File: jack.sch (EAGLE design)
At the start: 16 parts, among them IC1 NUF2221W1T2G

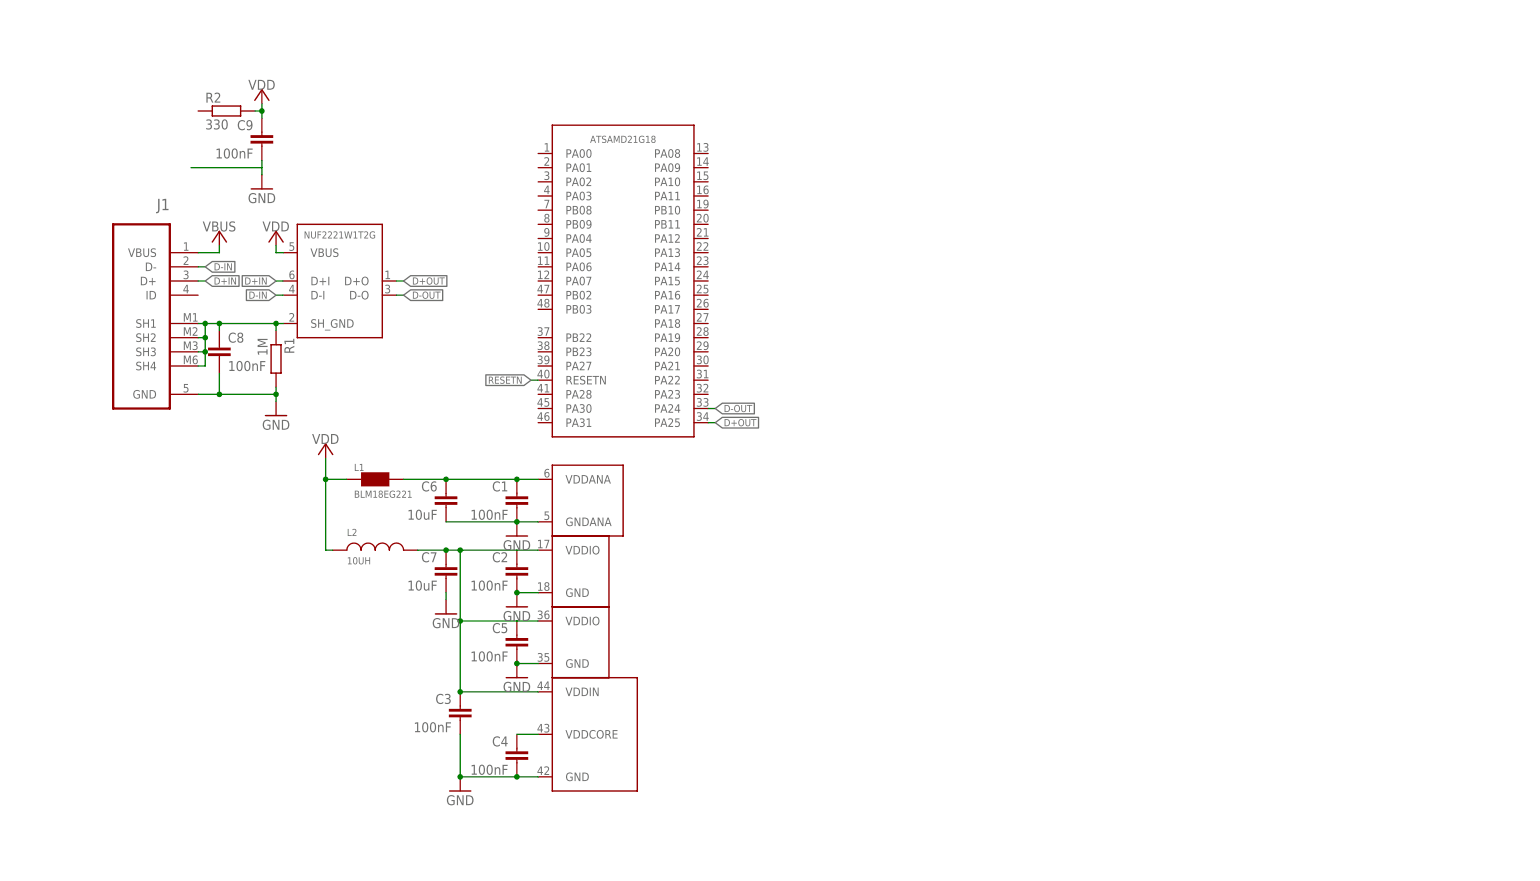
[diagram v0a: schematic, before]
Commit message: :grin: Added SPST symbol, modded SAMD21 pin names
Added SPST symbol for the reset switch (still got to find a suitable
tact switch), modified the SAMD21 pin names to show all their functions
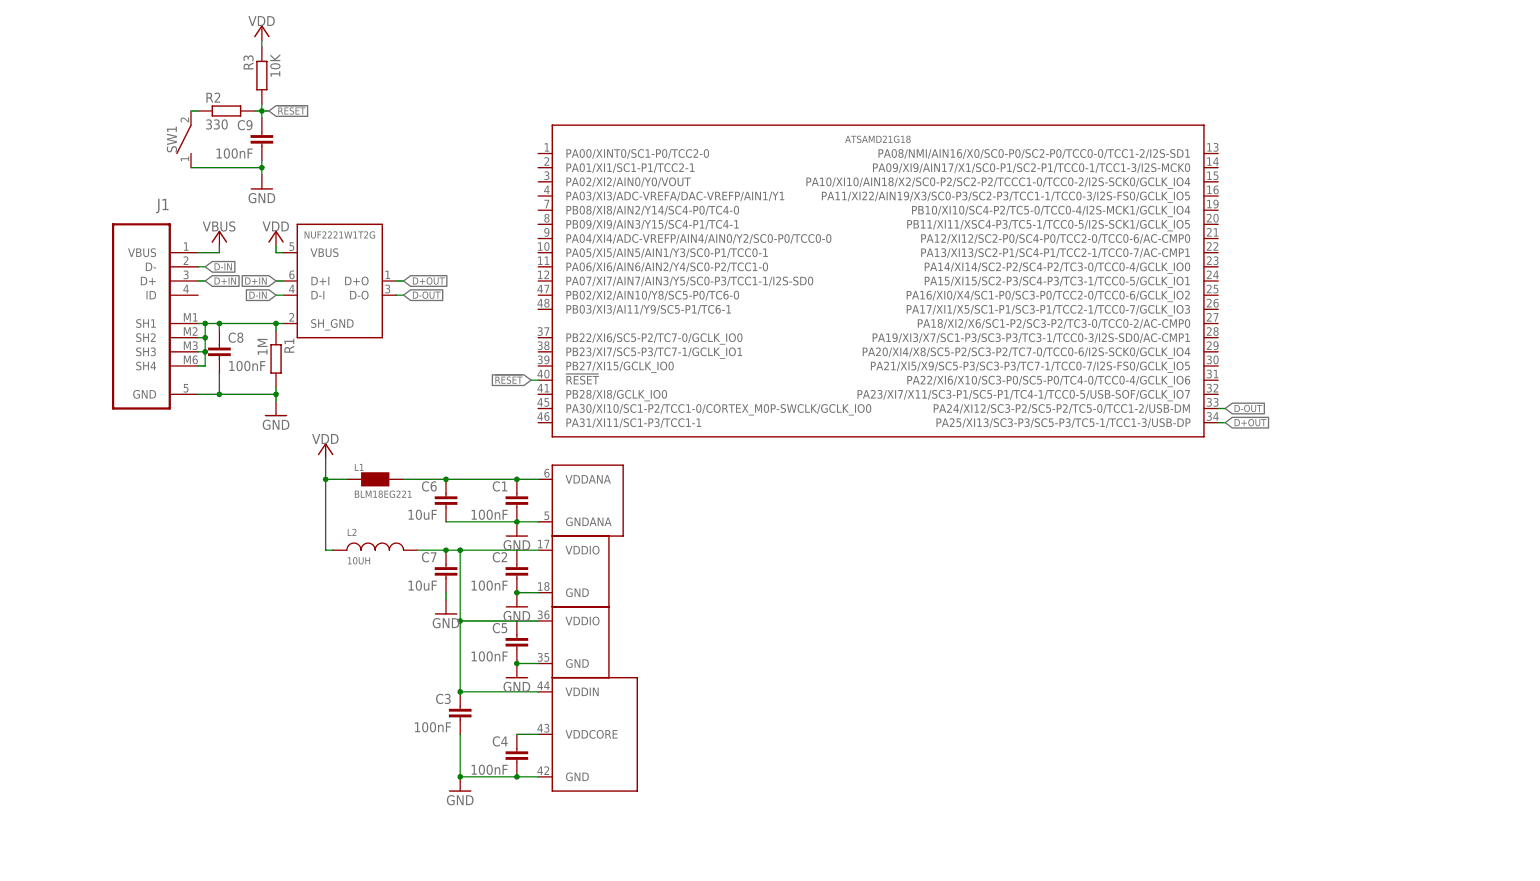
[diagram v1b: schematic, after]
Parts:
- removed U$1: ATSAMD21G18, jack:ATSAMD21G18
- added IC2: ATSAMD21G18, jack:ATSAMD21G18
- added R3: 10K, rcl:R-EU_R0603
- added SW1: SPST, jack:SPST
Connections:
- removed net RESETN: U$1IO.RESETN
- new net !RESET: C9.1, IC2IO.!RESET, R2.2, R3.2
- new net N$3: R2.1, SW1.P$2
- net D+OUT: now also IC2IO.PA25/XI13/SC3-P3/SC5-P3/TC5-1/TCC1-3/USB-DP; no longer U$1IO.PA25
- net D-OUT: now also IC2IO.PA24/XI12/SC3-P2/SC5-P2/TC5-0/TCC1-2/USB-DM; no longer U$1IO.PA24
- net GND: now also IC2PWR-ANA.GNDANA, IC2PWR-IN-CORE.GND, IC2PWR-IO1.GND, IC2PWR-IO2.GND, SW1.P$1; no longer U$1PWR-ANA.GNDANA, U$1PWR-IN-CORE.GND, U$1PWR-IO1.GND, U$1PWR-IO2.GND
- net N$1: now also IC2PWR-ANA.VDDANA; no longer U$1PWR-ANA.VDDANA
- net N$4: now also IC2PWR-IN-CORE.VDDIN, IC2PWR-IO1.VDDIO, IC2PWR-IO2.VDDIO; no longer U$1PWR-IN-CORE.VDDIN, U$1PWR-IO1.VDDIO, U$1PWR-IO2.VDDIO
- net VDD: now also R3.1; no longer C9.1, R2.2
- net VDDCORE: now also IC2PWR-IN-CORE.VDDCORE; no longer U$1PWR-IN-CORE.VDDCORE
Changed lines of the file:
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@@
 </classes>
 <parts>
-<part name="U$1" library="jack" deviceset="ATSAMD21G18" device=""/>
+<part name="IC2" library="jack" deviceset="ATSAMD21G18" device=""/>
 <part name="C1" library="rcl" deviceset="C-EU" device="C0603" value="100nF"/>
 <part name="C2" library="rcl" deviceset="C-EU" device="C0603" value="100nF"/>
@@
 <part name="GND7" library="cortexm0" deviceset="GND" device=""/>
 <part name="R2" library="rcl" deviceset="R-EU_" device="R0603" value="330"/>
+<part name="R3" library="rcl" deviceset="R-EU_" device="R0603" value="10K"/>
+<part name="SW1" library="jack" deviceset="SPST" device=""/>
 </parts>
 <sheets>
@@
 </plain>
 <instances>
-<instance part="U$1" gate="IO" x="0" y="0"/>
-<instance part="U$1" gate="PWR-ANA" x="-6.35" y="-39.37"/>
-<instance part="U$1" gate="PWR-IN-CORE" x="-5.08" y="-81.28"/>
-<instance part="U$1" gate="PWR-IO1" x="-7.62" y="-52.07"/>
-<instance part="U$1" gate="PWR-IO2" x="-7.62" y="-64.77"/>
+<instance part="IC2" gate="IO" x="45.72" y="0"/>
+<instance part="IC2" gate="PWR-ANA" x="-6.35" y="-39.37"/>
+<instance part="IC2" gate="PWR-IN-CORE" x="-5.08" y="-81.28"/>
+<instance part="IC2" gate="PWR-IO1" x="-7.62" y="-52.07"/>
+<instance part="IC2" gate="PWR-IO2" x="-7.62" y="-64.77"/>
 <instance part="C1" gate="G$1" x="-19.05" y="-38.1" rot="MR0"/>
 <instance part="C2" gate="G$1" x="-19.05" y="-50.8" rot="MR0"/>
@@
 <instance part="GND6" gate="G$1" x="-62.23" y="-21.59"/>
 <instance part="C9" gate="G$1" x="-64.77" y="26.67" rot="MR0"/>
-<instance part="VDD3" gate="G$1" x="-64.77" y="31.75"/>
+<instance part="VDD3" gate="G$1" x="-64.77" y="43.18"/>
 <instance part="GND7" gate="G$1" x="-64.77" y="19.05"/>
 <instance part="R2" gate="G$1" x="-71.12" y="30.48"/>
+<instance part="R3" gate="G$1" x="-64.77" y="36.83" rot="MR270"/>
+<instance part="SW1" gate="G$1" x="-77.47" y="25.4" rot="R90"/>
 </instances>
 <busses>
@@
 <net name="GND" class="0">
 <segment>
-<pinref part="U$1" gate="PWR-IO1" pin="GND"/>
+<pinref part="IC2" gate="PWR-IO1" pin="GND"/>
 <pinref part="C2" gate="G$1" pin="2"/>
 <wire x1="-15.24" y1="-55.88" x2="-19.05" y2="-55.88" width="0.1524" layer="91"/>
@@
 </segment>
 <segment>
-<pinref part="U$1" gate="PWR-IO2" pin="GND"/>
+<pinref part="IC2" gate="PWR-IO2" pin="GND"/>
 <pinref part="C5" gate="G$1" pin="2"/>
 <wire x1="-15.24" y1="-68.58" x2="-19.05" y2="-68.58" width="0.1524" layer="91"/>
@@
 </segment>
 <segment>
-<pinref part="U$1" gate="PWR-IN-CORE" pin="GND"/>
+<pinref part="IC2" gate="PWR-IN-CORE" pin="GND"/>
 <pinref part="C4" gate="G$1" pin="2"/>
 <wire x1="-15.24" y1="-88.9" x2="-19.05" y2="-88.9" width="0.1524" layer="91"/>
@@
 </segment>
 <segment>
-<pinref part="U$1" gate="PWR-ANA" pin="GNDANA"/>
+<pinref part="IC2" gate="PWR-ANA" pin="GNDANA"/>
 <pinref part="C1" gate="G$1" pin="2"/>
 <wire x1="-15.24" y1="-43.18" x2="-19.05" y2="-43.18" width="0.1524" layer="91"/>
@@
 <wire x1="-64.77" y1="20.32" x2="-64.77" y2="19.05" width="0.1524" layer="91"/>
 <wire x1="-64.77" y1="20.32" x2="-77.47" y2="20.32" width="0.1524" layer="91"/>
+<junction x="-64.77" y="20.32"/>
+<pinref part="SW1" gate="G$1" pin="P$1"/>
 </segment>
 </net>
 <net name="VDDCORE" class="0">
 <segment>
-<pinref part="U$1" gate="PWR-IN-CORE" pin="VDDCORE"/>
+<pinref part="IC2" gate="PWR-IN-CORE" pin="VDDCORE"/>
 <pinref part="C4" gate="G$1" pin="1"/>
 <wire x1="-15.24" y1="-81.28" x2="-19.05" y2="-81.28" width="0.1524" layer="91"/>
@@
 </segment>
 <segment>
-<pinref part="C9" gate="G$1" pin="1"/>
 <pinref part="VDD3" gate="G$1" pin="VDD"/>
-<wire x1="-64.77" y1="31.75" x2="-64.77" y2="30.48" width="0.1524" layer="91"/>
-<pinref part="R2" gate="G$1" pin="2"/>
-<wire x1="-64.77" y1="30.48" x2="-64.77" y2="29.21" width="0.1524" layer="91"/>
-<wire x1="-66.04" y1="30.48" x2="-64.77" y2="30.48" width="0.1524" layer="91"/>
-<junction x="-64.77" y="30.48"/>
+<pinref part="R3" gate="G$1" pin="1"/>
+<wire x1="-64.77" y1="43.18" x2="-64.77" y2="41.91" width="0.1524" layer="91"/>
 </segment>
 </net>
 <net name="N$1" class="0">
 <segment>
-<pinref part="U$1" gate="PWR-ANA" pin="VDDANA"/>
+<pinref part="IC2" gate="PWR-ANA" pin="VDDANA"/>
 <pinref part="C1" gate="G$1" pin="1"/>
 <wire x1="-15.24" y1="-35.56" x2="-19.05" y2="-35.56" width="0.1524" layer="91"/>
@@
 <net name="N$4" class="0">
 <segment>
-<pinref part="U$1" gate="PWR-IO2" pin="VDDIO"/>
+<pinref part="IC2" gate="PWR-IO2" pin="VDDIO"/>
 <pinref part="C5" gate="G$1" pin="1"/>
 <wire x1="-15.24" y1="-60.96" x2="-19.05" y2="-60.96" width="0.1524" layer="91"/>
@@
 <pinref part="C7" gate="G$1" pin="1"/>
 <wire x1="-31.75" y1="-48.26" x2="-36.83" y2="-48.26" width="0.1524" layer="91"/>
-<pinref part="U$1" gate="PWR-IO1" pin="VDDIO"/>
+<pinref part="IC2" gate="PWR-IO1" pin="VDDIO"/>
 <pinref part="C2" gate="G$1" pin="1"/>
 <wire x1="-15.24" y1="-48.26" x2="-19.05" y2="-48.26" width="0.1524" layer="91"/>
@@
 <wire x1="-29.21" y1="-48.26" x2="-19.05" y2="-48.26" width="0.1524" layer="91"/>
 <wire x1="-29.21" y1="-60.96" x2="-29.21" y2="-48.26" width="0.1524" layer="91"/>
-<pinref part="U$1" gate="PWR-IN-CORE" pin="VDDIN"/>
+<pinref part="IC2" gate="PWR-IN-CORE" pin="VDDIN"/>
 <pinref part="C3" gate="G$1" pin="1"/>
 <wire x1="-15.24" y1="-73.66" x2="-29.21" y2="-73.66" width="0.1524" layer="91"/>
@@
 <net name="D+OUT" class="0">
 <segment>
-<pinref part="U$1" gate="IO" pin="PA25"/>
-<wire x1="15.24" y1="-25.4" x2="16.51" y2="-25.4" width="0.1524" layer="91"/>
-<label x="16.51" y="-25.4" size="1.27" layer="95" xref="yes"/>
-</segment>
-<segment>
 <wire x1="-40.64" y1="0" x2="-39.37" y2="0" width="0.1524" layer="91"/>
 <label x="-39.37" y="0" size="1.27" layer="95" xref="yes"/>
 <pinref part="IC1" gate="G$1" pin="D+O"/>
 </segment>
+<segment>
+<pinref part="IC2" gate="IO" pin="PA25/XI13/SC3-P3/SC5-P3/TC5-1/TCC1-3/USB-DP"/>
+<wire x1="106.68" y1="-25.4" x2="107.95" y2="-25.4" width="0.1524" layer="91"/>
+<label x="107.95" y="-25.4" size="1.27" layer="95" xref="yes"/>
+</segment>
 </net>
 <net name="D-OUT" class="0">
-<segment>
-<pinref part="U$1" gate="IO" pin="PA24"/>
-<wire x1="15.24" y1="-22.86" x2="16.51" y2="-22.86" width="0.1524" layer="91"/>
-<label x="16.51" y="-22.86" size="1.27" layer="95" xref="yes"/>
-</segment>
 <segment>
 <wire x1="-40.64" y1="-2.54" x2="-39.37" y2="-2.54" width="0.1524" layer="91"/>
 <label x="-39.37" y="-2.54" size="1.27" layer="95" xref="yes"/>
 <pinref part="IC1" gate="G$1" pin="D-O"/>
+</segment>
+<segment>
+<pinref part="IC2" gate="IO" pin="PA24/XI12/SC3-P2/SC5-P2/TC5-0/TCC1-2/USB-DM"/>
+<wire x1="106.68" y1="-22.86" x2="107.95" y2="-22.86" width="0.1524" layer="91"/>
+<label x="107.95" y="-22.86" size="1.27" layer="95" xref="yes"/>
 </segment>
 </net>
@@
 </segment>
 </net>
-<net name="RESETN" class="0">
-<segment>
-<pinref part="U$1" gate="IO" pin="RESETN"/>
+<net name="!RESET" class="0">
+<segment>
+<pinref part="IC2" gate="IO" pin="!RESET"/>
 <wire x1="-15.24" y1="-17.78" x2="-16.51" y2="-17.78" width="0.1524" layer="91"/>
 <label x="-16.51" y="-17.78" size="1.27" layer="95" rot="R180" xref="yes"/>
 </segment>
-</net>
+<segment>
+<pinref part="C9" gate="G$1" pin="1"/>
+<pinref part="R2" gate="G$1" pin="2"/>
+<wire x1="-64.77" y1="30.48" x2="-64.77" y2="29.21" width="0.1524" layer="91"/>
+<wire x1="-66.04" y1="30.48" x2="-64.77" y2="30.48" width="0.1524" layer="91"/>
+<junction x="-64.77" y="30.48"/>
+<wire x1="-64.77" y1="30.48" x2="-63.5" y2="30.48" width="0.1524" layer="91"/>
+<pinref part="R3" gate="G$1" pin="2"/>
+<wire x1="-64.77" y1="31.75" x2="-64.77" y2="30.48" width="0.1524" layer="91"/>
+<label x="-63.5" y="30.48" size="1.27" layer="95" xref="yes"/>
+</segment>
+</net>
+<net name="N$3" class="0">
+<segment>
+<pinref part="R2" gate="G$1" pin="1"/>
+<wire x1="-76.2" y1="30.48" x2="-77.47" y2="30.48" width="0.1524" layer="91"/>
+<pinref part="SW1" gate="G$1" pin="P$2"/>
+</segment>
+</net>

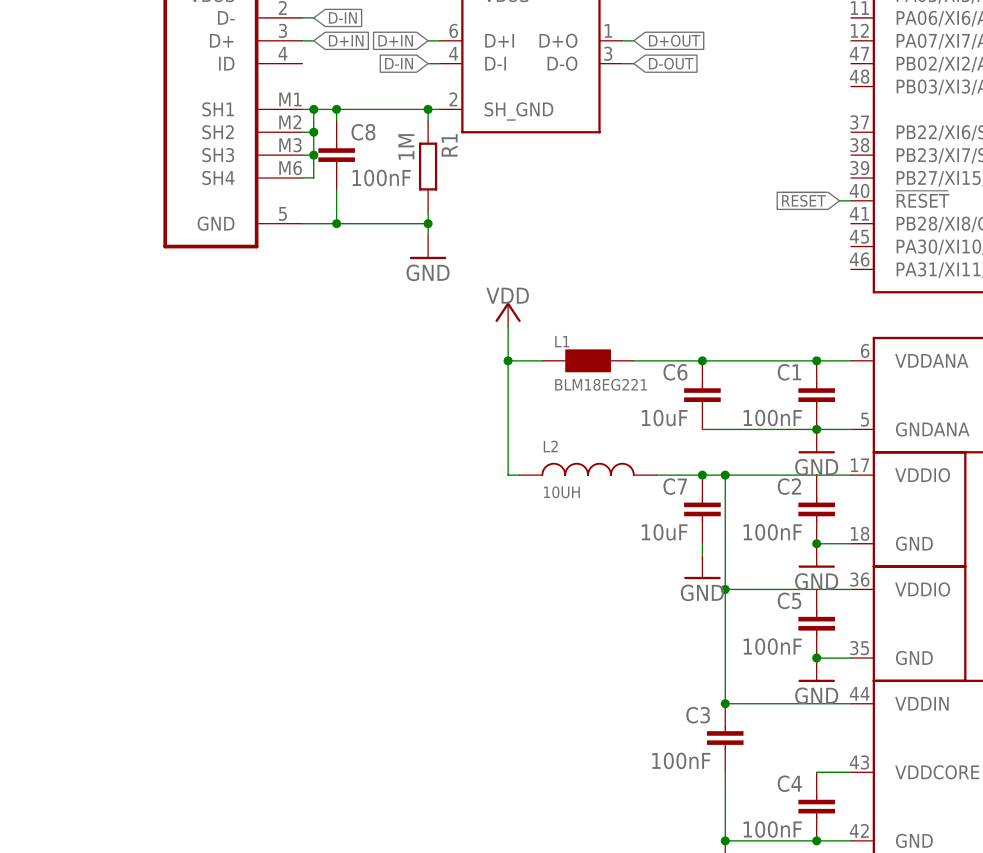
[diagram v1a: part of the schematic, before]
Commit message: :+1:  Added LDO and graphics
Added 3.3 V LDO in library and schematic, added graphics for logo
(temporary?)
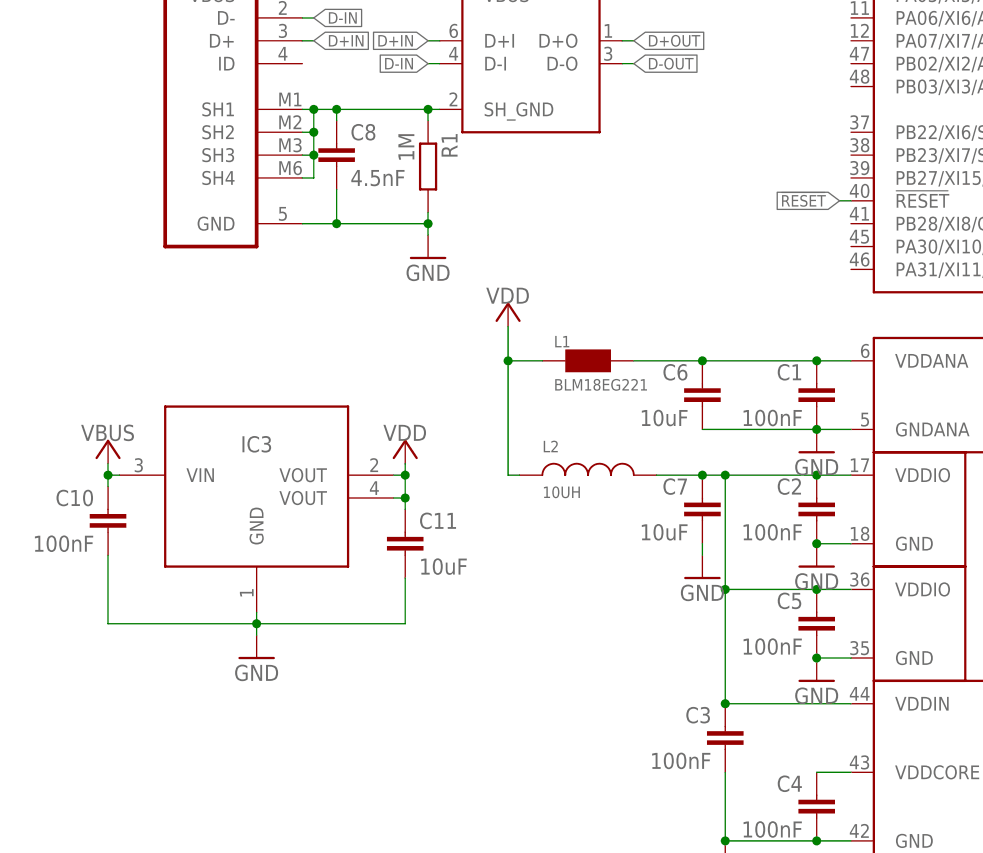
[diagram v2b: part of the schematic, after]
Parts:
- added C10: 100nF, rcl:C-EUC0603
- added C11: 10uF, rcl:C-EUC0603
- added IC3: LDO, jack:LDO
- C8: value 100nF -> 4.5nF
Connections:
- net GND: now also C10.2, C11.2, IC3.GND
- net VBUS: now also C10.1, IC3.VIN
- net VDD: now also C11.1, IC3.VOUT@1, IC3.VOUT@2
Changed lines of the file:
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@@
 <part name="L2" library="Panasonic-ELL" deviceset="ELL" device="-VXG" technology="VFG100MC" value="10UH"/>
 <part name="J1" library="Molex-47346-0001" deviceset="47346-0001" device=""/>
-<part name="C8" library="rcl" deviceset="C-EU" device="C0603" value="100nF"/>
+<part name="C8" library="rcl" deviceset="C-EU" device="C0603" value="4.5nF"/>
 <part name="R1" library="rcl" deviceset="R-EU_" device="R0603" value="1M"/>
 <part name="IC1" library="jack" deviceset="NUF2221W1T2G" device=""/>
@@
 <part name="R3" library="rcl" deviceset="R-EU_" device="R0603" value="10K"/>
 <part name="SW1" library="jack" deviceset="SPST" device=""/>
+<part name="IC3" library="jack" deviceset="LDO" device=""/>
+<part name="VDD4" library="jack" deviceset="VDD" device=""/>
+<part name="VBUS2" library="jack" deviceset="VBUS" device=""/>
+<part name="GND8" library="cortexm0" deviceset="GND" device=""/>
+<part name="C10" library="rcl" deviceset="C-EU" device="C0603" value="100nF"/>
+<part name="C11" library="rcl" deviceset="C-EU" device="C0603" value="10uF"/>
 </parts>
 <sheets>
@@
 <instance part="R3" gate="G$1" x="-64.77" y="36.83" rot="MR270"/>
 <instance part="SW1" gate="G$1" x="-77.47" y="25.4" rot="R90"/>
+<instance part="IC3" gate="G$1" x="-81.28" y="-48.26"/>
+<instance part="VDD4" gate="G$1" x="-64.77" y="-46.99"/>
+<instance part="VBUS2" gate="G$1" x="-97.79" y="-46.99"/>
+<instance part="GND8" gate="G$1" x="-81.28" y="-66.04"/>
+<instance part="C10" gate="G$1" x="-97.79" y="-52.07" rot="MR0"/>
+<instance part="C11" gate="G$1" x="-64.77" y="-54.61"/>
 </instances>
 <busses>
@@
 <pinref part="SW1" gate="G$1" pin="P$1"/>
 </segment>
+<segment>
+<pinref part="IC3" gate="G$1" pin="GND"/>
+<pinref part="GND8" gate="G$1" pin="GND"/>
+<wire x1="-81.28" y1="-66.04" x2="-81.28" y2="-64.77" width="0.1524" layer="91"/>
+<pinref part="C10" gate="G$1" pin="2"/>
+<wire x1="-81.28" y1="-64.77" x2="-81.28" y2="-63.5" width="0.1524" layer="91"/>
+<wire x1="-97.79" y1="-57.15" x2="-97.79" y2="-64.77" width="0.1524" layer="91"/>
+<wire x1="-97.79" y1="-64.77" x2="-81.28" y2="-64.77" width="0.1524" layer="91"/>
+<pinref part="C11" gate="G$1" pin="2"/>
+<wire x1="-64.77" y1="-59.69" x2="-64.77" y2="-64.77" width="0.1524" layer="91"/>
+<wire x1="-64.77" y1="-64.77" x2="-81.28" y2="-64.77" width="0.1524" layer="91"/>
+<junction x="-81.28" y="-64.77"/>
+</segment>
 </net>
 <net name="VDDCORE" class="0">
@@
 <pinref part="R3" gate="G$1" pin="1"/>
 <wire x1="-64.77" y1="43.18" x2="-64.77" y2="41.91" width="0.1524" layer="91"/>
+</segment>
+<segment>
+<pinref part="VDD4" gate="G$1" pin="VDD"/>
+<pinref part="C11" gate="G$1" pin="1"/>
+<wire x1="-64.77" y1="-46.99" x2="-64.77" y2="-48.26" width="0.1524" layer="91"/>
+<pinref part="IC3" gate="G$1" pin="VOUT@1"/>
+<wire x1="-64.77" y1="-48.26" x2="-64.77" y2="-50.8" width="0.1524" layer="91"/>
+<wire x1="-64.77" y1="-50.8" x2="-64.77" y2="-52.07" width="0.1524" layer="91"/>
+<wire x1="-66.04" y1="-48.26" x2="-64.77" y2="-48.26" width="0.1524" layer="91"/>
+<pinref part="IC3" gate="G$1" pin="VOUT@2"/>
+<wire x1="-66.04" y1="-50.8" x2="-64.77" y2="-50.8" width="0.1524" layer="91"/>
+<junction x="-64.77" y="-48.26"/>
+<junction x="-64.77" y="-50.8"/>
 </segment>
 </net>
@@
 <junction x="-31.75" y="-48.26"/>
 <pinref part="L2" gate="A" pin="1"/>
+<junction x="-19.05" y="-60.96"/>
+<junction x="-19.05" y="-48.26"/>
 </segment>
 </net>
@@
 <wire x1="-72.39" y1="5.08" x2="-72.39" y2="6.35" width="0.1524" layer="91"/>
 </segment>
-</net>
+<segment>
+<pinref part="VBUS2" gate="G$1" pin="VBUS"/>
+<pinref part="C10" gate="G$1" pin="1"/>
+<wire x1="-97.79" y1="-46.99" x2="-97.79" y2="-48.26" width="0.1524" layer="91"/>
+<pinref part="IC3" gate="G$1" pin="VIN"/>
+<wire x1="-97.79" y1="-48.26" x2="-97.79" y2="-49.53" width="0.1524" layer="91"/>
+<wire x1="-97.79" y1="-48.26" x2="-96.52" y2="-48.26" width="0.1524" layer="91"/>
+<junction x="-97.79" y="-48.26"/>
+</segment>
+</net>
